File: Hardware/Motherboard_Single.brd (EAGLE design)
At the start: 86.4 x 73.7 mm, 88 parts, among them J1 MICROMOD-2222-C, J10 MICRO-SD-PUSH-PUSH-EXT-PIN, J2 Vertical Qwiic Connector, J4 QWIIC_RIGHT_ANGLE, J5 CORTEX_JTAG_DEBUG_MINIMUM_PTH, J6 MICROMOD_CARRIER, Q1 3.1A/30V/105mΩ, U2 MCP73831, U5 AP7361C-33

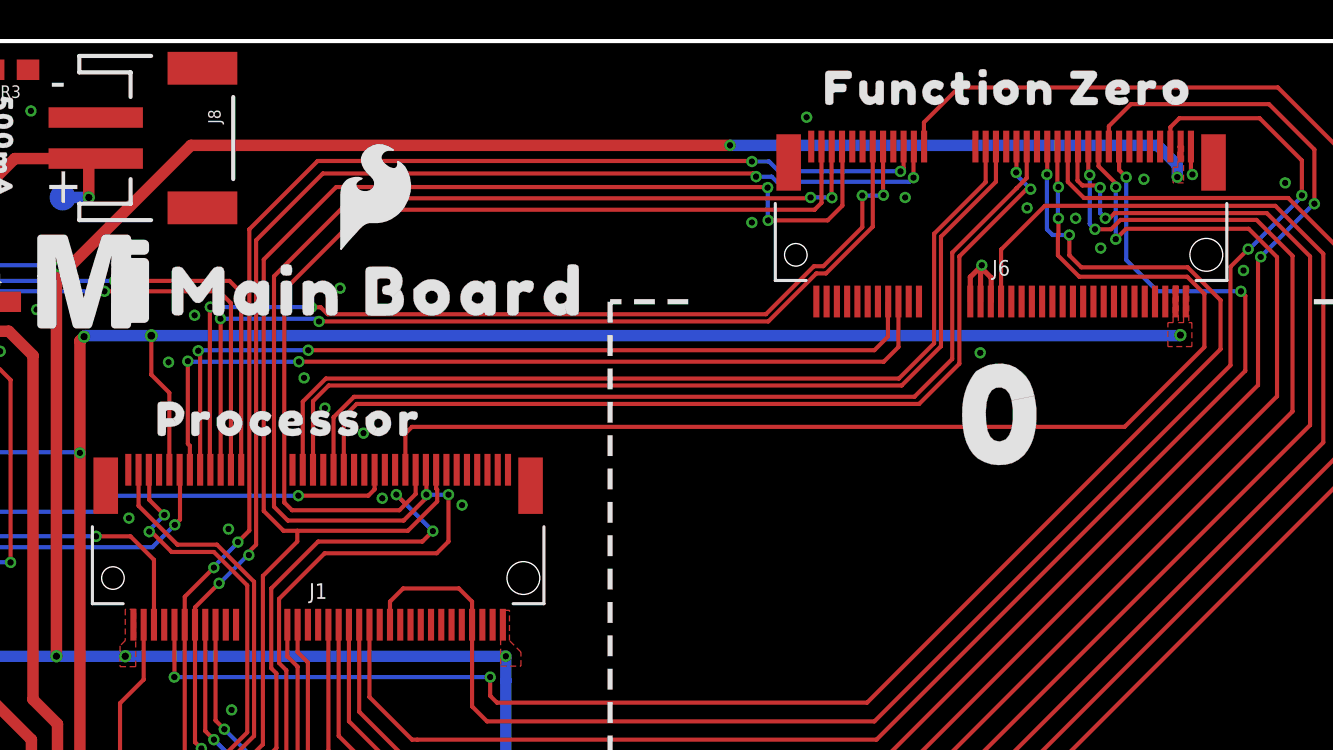
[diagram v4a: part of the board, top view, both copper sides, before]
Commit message: Adds prod_id to function board connector, double routes power enable to A1 and previous pin
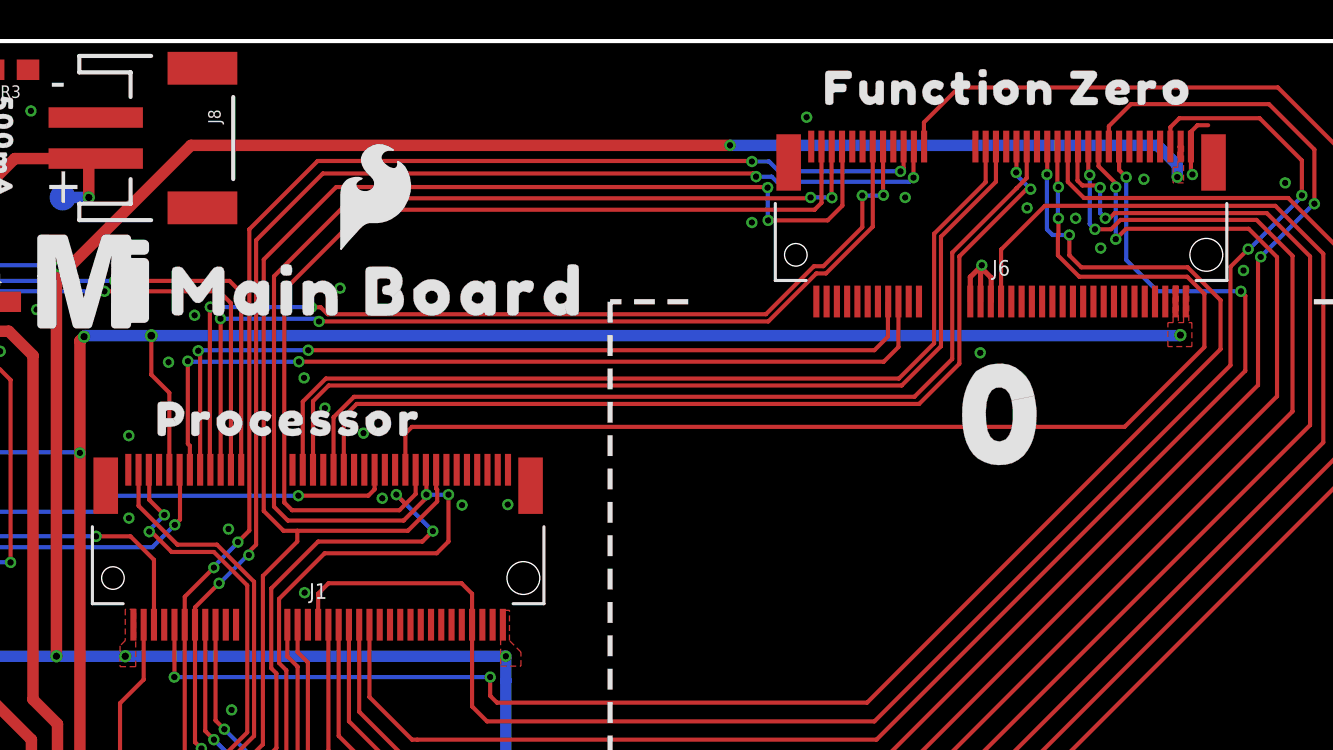
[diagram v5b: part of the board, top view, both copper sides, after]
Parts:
- H3, H4, H8: value STAND-OFF-REFLOW2.5MM_TALL -> STAND-OFF-REFLOW-M2.5_2.5MM_TALL
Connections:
- net PWR_EN0: now also J1.38; no longer J1.52
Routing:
- net PWR_EN0: track 75.0 -> 79.2 mm
- net GND: track 9.48 -> 11.2 mm, vias 56 -> 59
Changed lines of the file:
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@@
 <setting verticaltext="up"/>
 </settings>
-<grid distance="0.05" unitdist="inch" unit="inch" style="dots" multiple="1" display="yes" altdistance="0.005" altunitdist="inch" altunit="inch"/>
+<grid distance="0.5" unitdist="mm" unit="mm" style="dots" multiple="1" display="yes" altdistance="0.01" altunitdist="mm" altunit="mm"/>
 <layers>
 <layer number="1" name="Top" color="4" fill="1" visible="yes" active="yes"/>
@@
 <attribute name="REV" value="" x="16.51" y="-25.4" size="1.778" layer="27" font="vector" ratio="15" display="off"/>
 </element>
-<element name="H3" library="SparkFun-Hardware" package="STAND-OFF-REFLOW-M2.5" value="STAND-OFF-REFLOW2.5MM_TALL" x="81.28" y="21.0058" smashed="yes" rot="R270">
+<element name="H3" library="SparkFun-Hardware" package="STAND-OFF-REFLOW-M2.5" value="STAND-OFF-REFLOW-M2.5_2.5MM_TALL" x="81.28" y="21.0058" smashed="yes" rot="R270">
 <attribute name="PROD_ID" value="HW-14899" x="81.28" y="21.0058" size="2.54" layer="27" font="vector" ratio="15" rot="R270" display="off"/>
 </element>
-<element name="H8" library="SparkFun-Hardware" package="STAND-OFF-REFLOW-M2.5" value="STAND-OFF-REFLOW2.5MM_TALL" x="24.9682" y="27.2542" smashed="yes" rot="R270">
+<element name="H8" library="SparkFun-Hardware" package="STAND-OFF-REFLOW-M2.5" value="STAND-OFF-REFLOW-M2.5_2.5MM_TALL" x="24.9682" y="27.2542" smashed="yes" rot="R270">
 <attribute name="PROD_ID" value="HW-14899" x="24.9682" y="27.2542" size="2.54" layer="27" font="vector" ratio="15" rot="R270" display="off"/>
 </element>
@@
 <element name="J6" library="SparkFun-MicroMod-Function" package="M.2-CONNECTOR-E-FUNCTION-STANDARD" value="MICROMOD_CARRIER" x="62.23" y="63.246" smashed="yes" rot="R180">
 <attribute name="NAME" x="62.23" y="62.611" size="0.762" layer="25" rot="R180" align="center"/>
+<attribute name="PROD_ID" value="CONN-14877" x="62.23" y="63.246" size="1.778" layer="27" rot="R180" display="off"/>
 <attribute name="VALUE" x="62.23" y="63.881" size="0.762" layer="27" rot="R180" align="center"/>
 </element>
@@
 <attribute name="VALUE" x="24.9936" y="16.8148" size="0.6096" layer="27" font="vector" ratio="20" rot="R90" align="top-center"/>
 </element>
-<element name="H4" library="SparkFun-Hardware" package="STAND-OFF-REFLOW-M2.5" value="STAND-OFF-REFLOW2.5MM_TALL" x="43.18" y="20.9804" smashed="yes" rot="R270">
+<element name="H4" library="SparkFun-Hardware" package="STAND-OFF-REFLOW-M2.5" value="STAND-OFF-REFLOW-M2.5_2.5MM_TALL" x="43.18" y="20.9804" smashed="yes" rot="R270">
 <attribute name="PROD_ID" value="HW-14899" x="43.18" y="20.9804" size="1.778" layer="27" rot="R270" display="off"/>
 </element>
@@
 <via x="15.8496" y="16.1544" extent="1-16" drill="0.3048"/>
 <contactref element="R6" pad="1"/>
+<via x="28.2956" y="46.7868" extent="1-16" drill="0.3048"/>
+<via x="38.1956" y="51.0768" extent="1-16" drill="0.3048"/>
+<via x="19.7344" y="54.4368" extent="1-16" drill="0.3048"/>
+<wire x1="71.48" y1="68.521" x2="71.48" y2="69.24" width="0.2032" layer="1"/>
+<wire x1="71.8" y1="69.56" x2="72.32" y2="69.56" width="0.2032" layer="1"/>
+<wire x1="71.48" y1="69.24" x2="71.8" y2="69.56" width="0.2032" layer="1"/>
 </signal>
 <signal name="V_BATT" class="1">
@@
 <wire x1="37.1856" y1="40.513" x2="56.0578" y2="40.513" width="0.2032" layer="1"/>
 <wire x1="56.0578" y1="40.513" x2="73.406" y2="57.8612" width="0.2032" layer="1"/>
-<contactref element="J1" pad="52"/>
-<wire x1="36.456" y1="45.223" x2="36.456" y2="46.348" width="0.2032" layer="1"/>
-<wire x1="32.456" y1="46.3498" x2="32.456" y2="45.223" width="0.2032" layer="1"/>
-<wire x1="36.456" y1="46.348" x2="35.814" y2="46.99" width="0.2032" layer="1"/>
-<wire x1="35.814" y1="46.99" x2="33.0962" y2="46.99" width="0.2032" layer="1"/>
-<wire x1="33.0962" y1="46.99" x2="32.456" y2="46.3498" width="0.2032" layer="1"/>
+<contactref element="J1" pad="38"/>
+<wire x1="36.456" y1="45.223" x2="36.456" y2="46.729" width="0.2032" layer="1"/>
+<wire x1="36.456" y1="46.729" x2="35.941" y2="47.244" width="0.2032" layer="1"/>
+<wire x1="29.464" y1="47.244" x2="28.956" y2="46.736" width="0.2032" layer="1"/>
+<wire x1="28.956" y1="46.736" x2="28.956" y2="45.223" width="0.2032" layer="1"/>
+<wire x1="35.941" y1="47.244" x2="29.464" y2="47.244" width="0.2032" layer="1"/>
 </signal>
 <signal name="I2C_SCL">

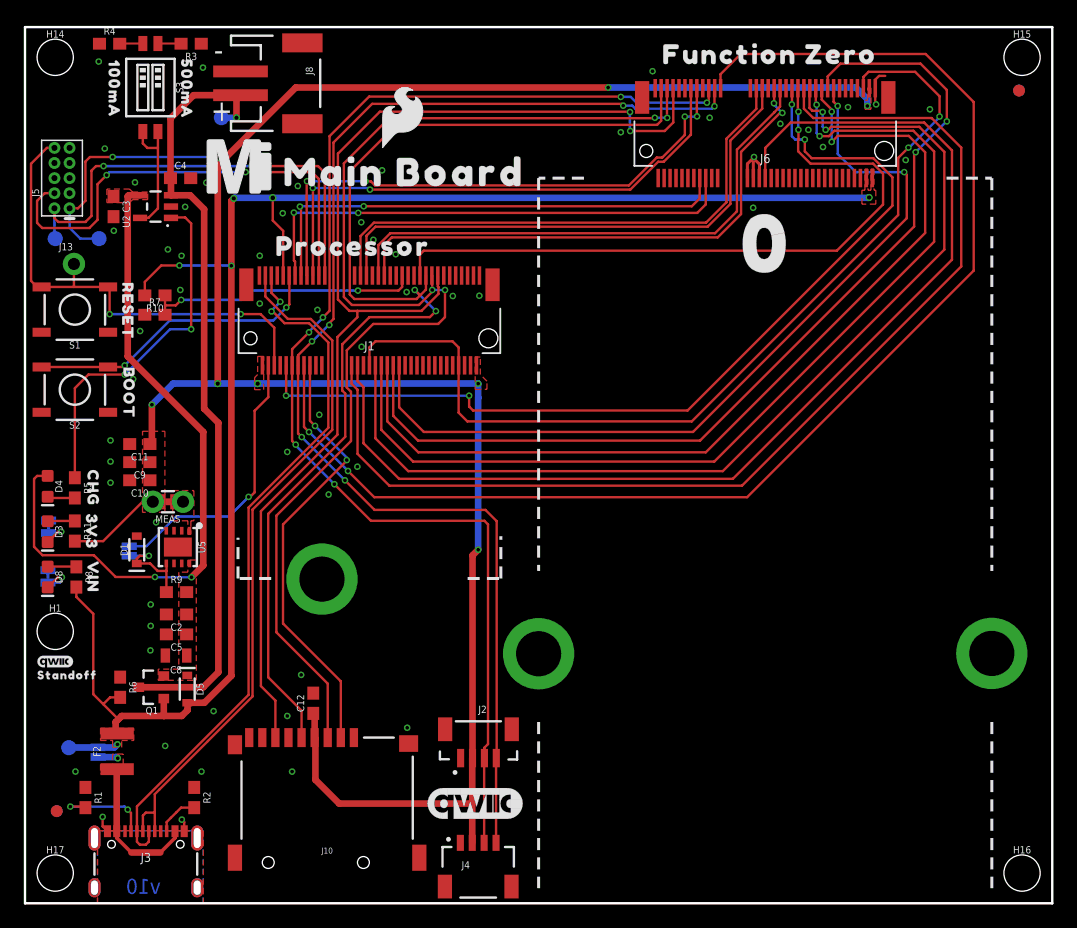
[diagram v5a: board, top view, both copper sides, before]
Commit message: Moves SD Card slightly towards center of PCB
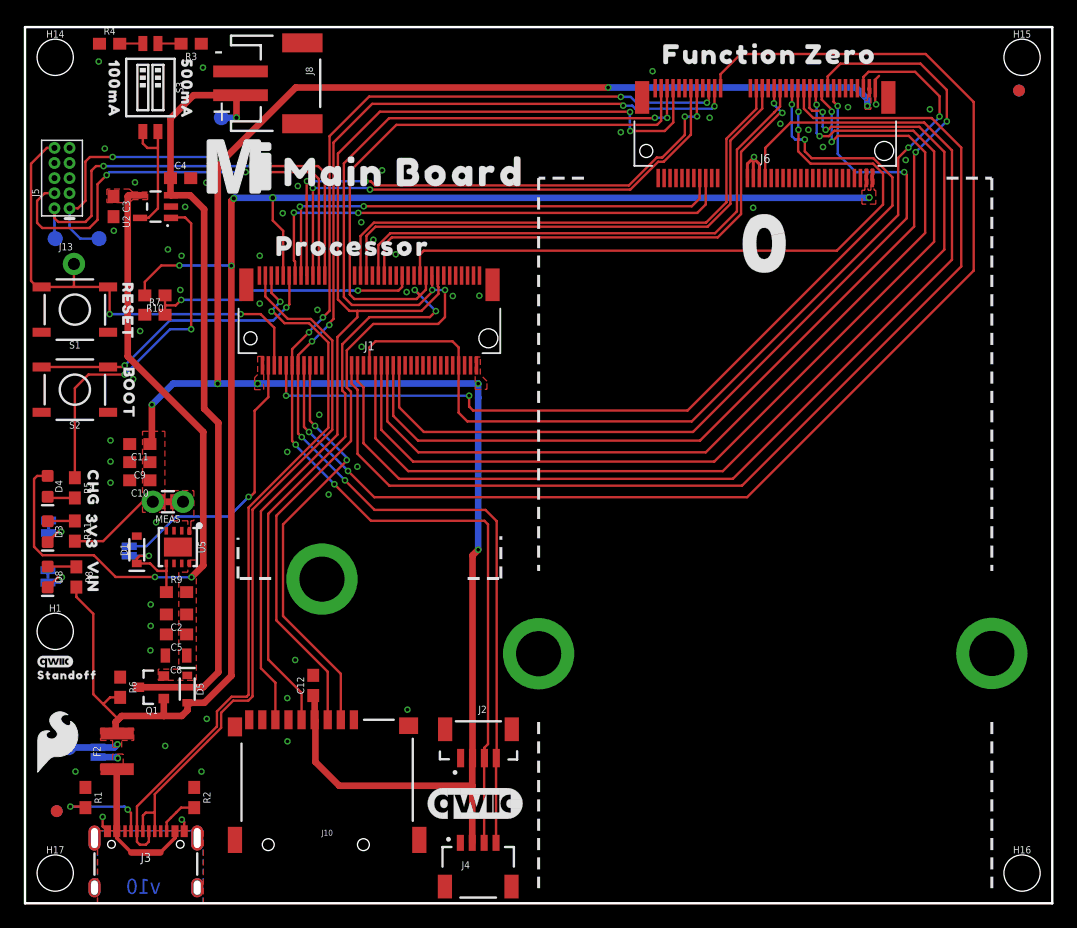
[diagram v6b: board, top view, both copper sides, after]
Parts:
- moved U$22 60.0 mm to (2.75, 13.5)
- moved J10 1.50 mm to (25.4, 4.93)
- moved C12 1.50 mm to (24.2, 18.3)
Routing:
- net SPI_PROCESSOR_SDI: track 97.4 -> 95.9 mm
- net SPI_PROCESSOR_SCK: track 98.3 -> 96.8 mm
- net D1-PROCESSOR/SD_CARD_!CS!: track 36.8 -> 35.3 mm
- net SPI_PROCESSOR_SDO: track 101.9 -> 100.4 mm
- net D+: track 58.8 -> 59.5 mm
- net D-: track 60.2 -> 61.0 mm
- net GND: track 11.2 -> 10.6 mm
